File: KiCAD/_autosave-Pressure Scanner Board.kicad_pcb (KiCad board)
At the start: 2 copper layers, 90 x 85 mm, 53 parts, among them J1 Cortex_Debug, J2 USB_Micro_B, J3 Battery Headers, J4 Can Header, Q1 3.7A, 30V, Q2 BSS138, Q3 BSS138, SW1 FSMCTTR, U1 SAMD21G18A-AU, U11 DLHR-L10D-E1BD-C-NAV8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

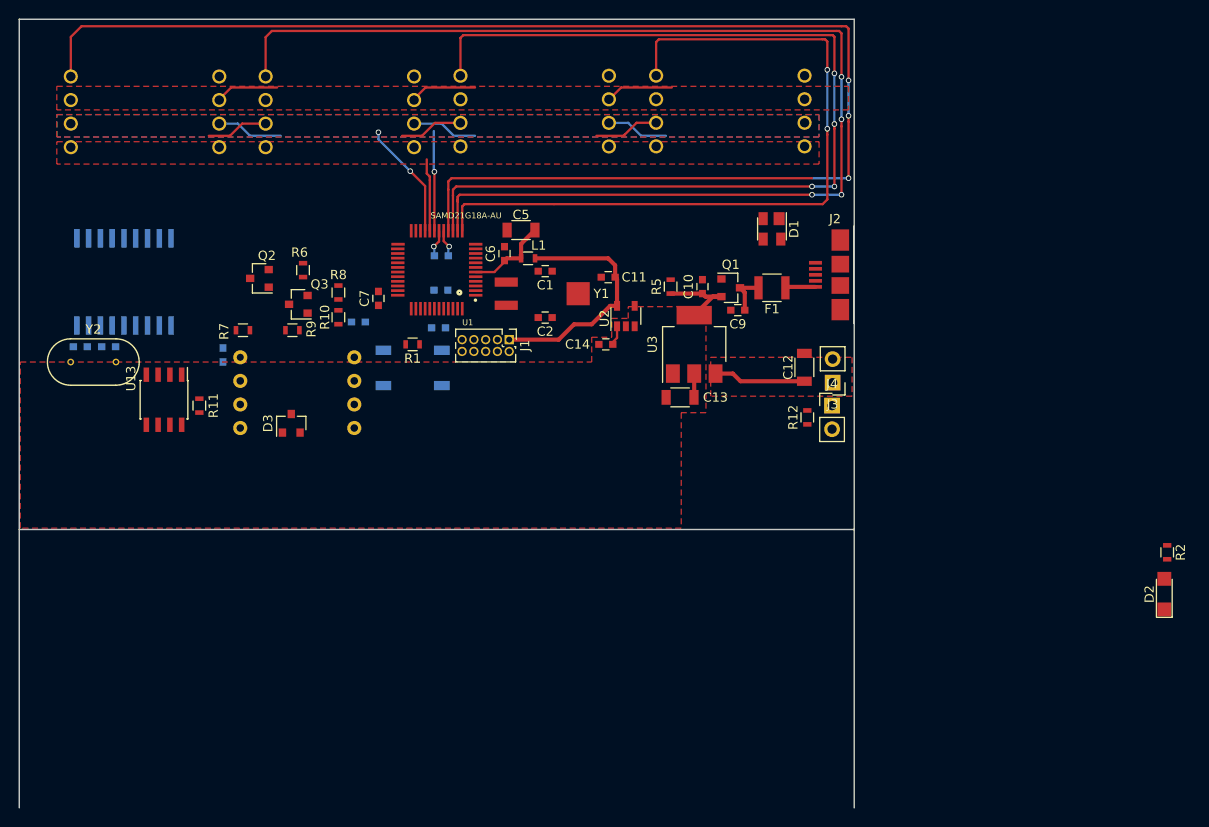
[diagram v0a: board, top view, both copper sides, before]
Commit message: Dropped 4 spare sensors, revising layout.
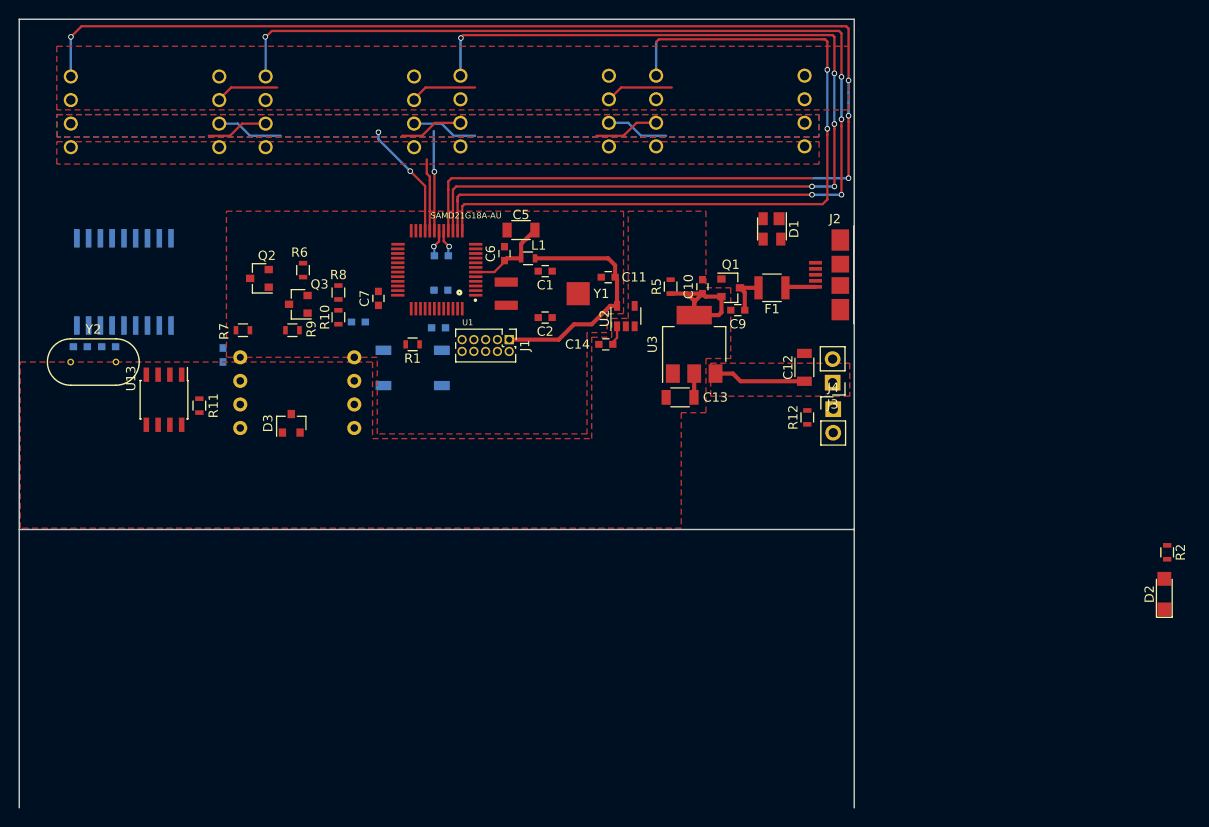
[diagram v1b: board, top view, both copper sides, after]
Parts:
- moved J4 0.40 mm to (197.7, 97.0)
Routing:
- net +5V: track 14.1 -> 20.4 mm
- net SS_1: track 129.3 -> 129.4 mm, vias 4 -> 5
- net SS_2: track 106.4 -> 106.5 mm, vias 4 -> 5
- net SS_3: vias 3 -> 4
